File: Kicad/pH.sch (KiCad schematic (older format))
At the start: 3 parts, among them U1 MCP6241

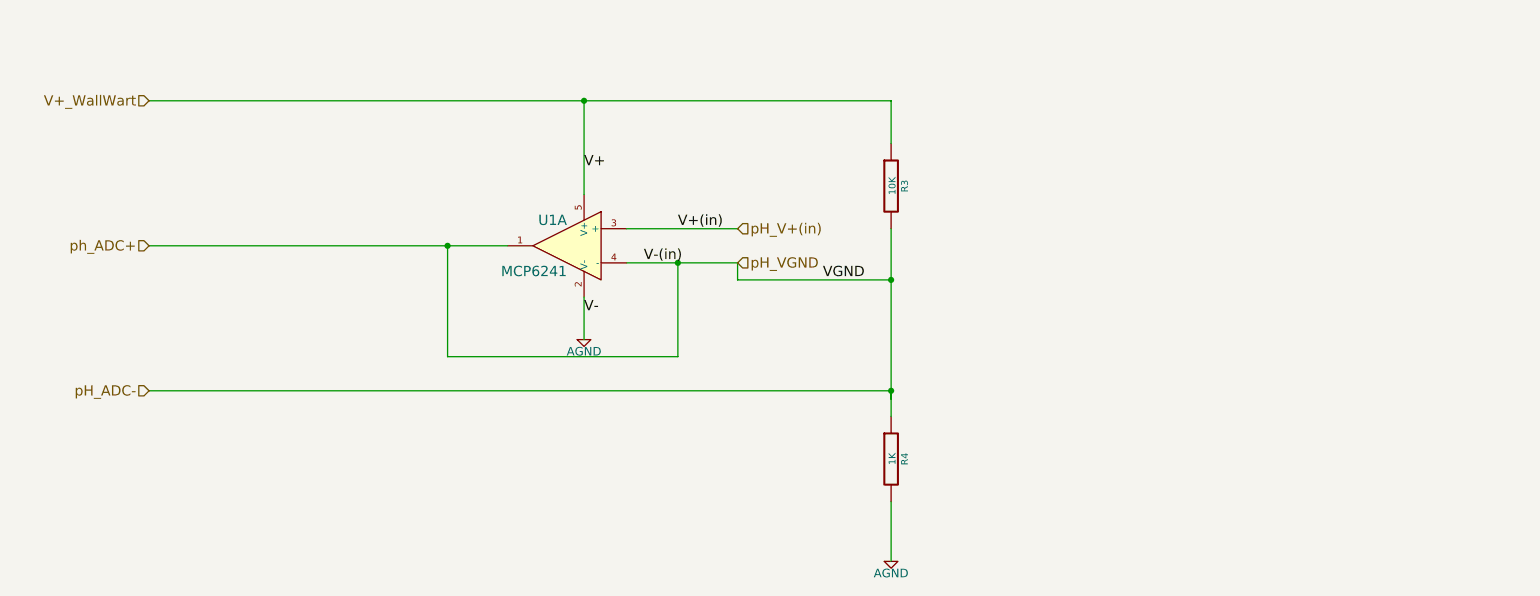
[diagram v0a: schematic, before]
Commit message: Layout with traces - ran through ERC and DRC
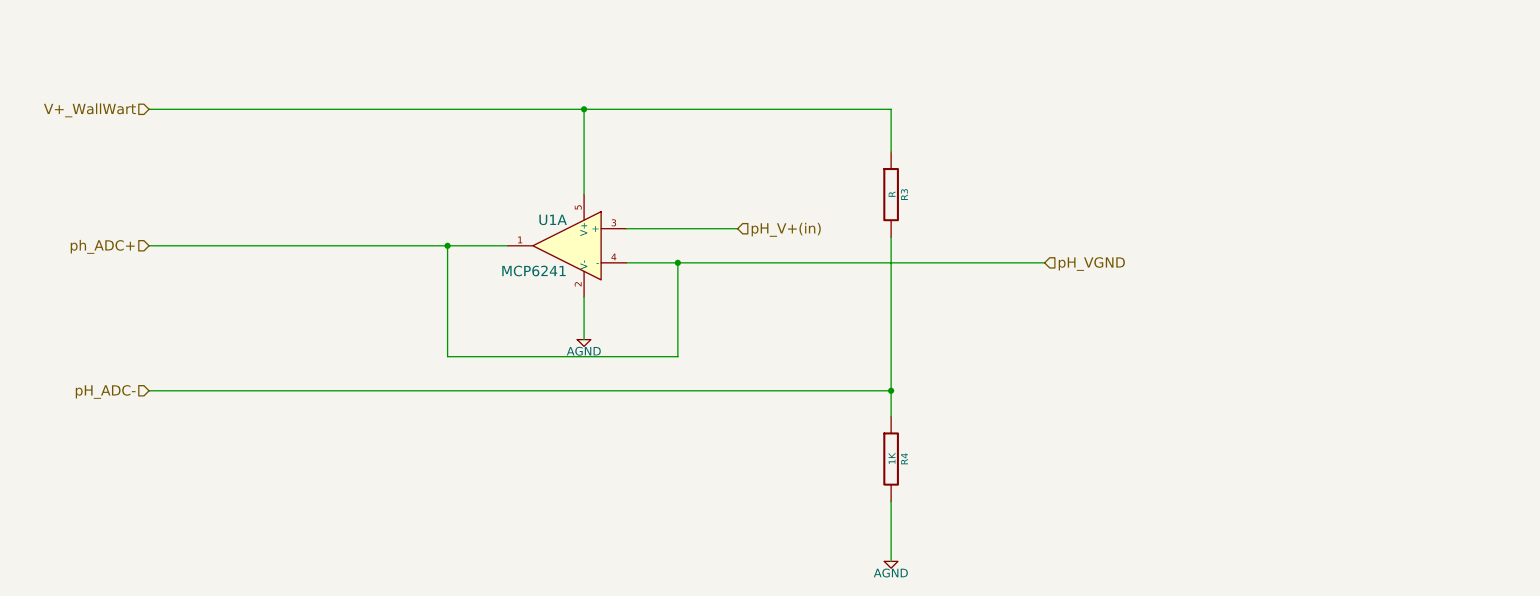
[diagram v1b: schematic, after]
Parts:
- R3: value 10K -> R
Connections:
- net labels removed: V+, V+(in), V-, V-(in), VGND
- wire segments 16 -> 13
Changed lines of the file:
@@
 Sheet 3 7
 Title ""
-Date "14 aug 2014"
+Date "19 aug 2014"
 Rev ""
 Comp ""
@@
 Comment4 ""
 $EndDescr
-Text HLabel 1350 2350 0    60   Input ~ 0
+Text HLabel 1350 2400 0    60   Input ~ 0
 V+_WallWart
 Text HLabel 1350 3200 0    60   Input ~ 0
@@
 	4450 3300 4450 3850
 Wire Wire Line
-	4150 3300 4800 3300
+	4150 3300 6600 3300
 Wire Wire Line
 	3900 3500 3900 3750
 Connection ~ 3100 3200
-Wire Wire Line
-	5700 2350 5700 2600
-$Comp
-L R R3
-U 1 1 53D7D144
-P 5700 2850
-F 0 "R3" V 5780 2850 40  0000 C CNN
-F 1 "10K" V 5707 2851 40  0000 C CNN
-F 2 "~" V 5630 2850 30  0000 C CNN
-F 3 "~" H 5700 2850 30  0000 C CNN
-	1    5700 2850
-	1    0    0    -1
-$EndComp
 $Comp
 L R R4
@@
 $EndComp
 Wire Wire Line
-	5700 3100 5700 4200
-Wire Wire Line
 	1350 3200 3450 3200
 Wire Wire Line
@@
 Text HLabel 1350 4050 0    60   Input ~ 0
 pH_ADC-
-Wire Wire Line
-	5700 4050 5700 4100
-Wire Wire Line
-	1350 4050 5700 4050
-Connection ~ 5700 4050
 $Comp
-L AGND #PWR8
+L AGND #PWR08
 U 1 1 53DCC7DA
 P 3900 3750
-F 0 "#PWR8" H 3900 3750 40  0001 C CNN
+F 0 "#PWR08" H 3900 3750 40  0001 C CNN
 F 1 "AGND" H 3900 3680 50  0000 C CNN
 F 2 "" H 3900 3750 60  0000 C CNN
@@
 $EndComp
 $Comp
-L AGND #PWR9
+L AGND #PWR09
 U 1 1 53DCC7F8
 P 5700 5050
-F 0 "#PWR9" H 5700 5050 40  0001 C CNN
+F 0 "#PWR09" H 5700 5050 40  0001 C CNN
 F 1 "AGND" H 5700 4980 50  0000 C CNN
 F 2 "" H 5700 5050 60  0000 C CNN
@@
 	1    0    0    -1
 $EndComp
-Wire Wire Line
-	1350 2350 5700 2350
-Wire Wire Line
-	3900 2350 3900 2900
-Connection ~ 3900 2350
-Text Label 5300 3400 0    60   ~ 0
-VGND
-Text Label 4450 3100 0    60   ~ 0
-V+(in)
-Text Label 3900 2750 0    60   ~ 0
-V+
-Text Label 3900 3600 0    60   ~ 0
-V-
-Text Label 4250 3300 0    60   ~ 0
-V-(in)
-Wire Wire Line
-	4800 3300 4800 3400
-Wire Wire Line
-	4800 3400 5700 3400
-Connection ~ 5700 3400
 Text HLabel 4800 3100 2    60   Input ~ 0
 pH_V+(in)
-Text HLabel 4800 3300 2    60   Input ~ 0
+Text HLabel 6600 3300 2    60   Input ~ 0
 pH_VGND
 Connection ~ 4450 3300
@@
 	-1   0    0    -1
 $EndComp
+$Comp
+L R R3
+U 1 1 53F37946
+P 5700 2900
+F 0 "R3" V 5780 2900 40  0000 C CNN
+F 1 "R" V 5707 2901 40  0000 C CNN
+F 2 "~" V 5630 2900 30  0000 C CNN
+F 3 "~" H 5700 2900 30  0000 C CNN
+	1    5700 2900
+	1    0    0    -1
+$EndComp
+Wire Wire Line
+	5700 3150 5700 4200
+Wire Wire Line
+	5700 2650 5700 2400
+Wire Wire Line
+	5700 2400 1350 2400
+Wire Wire Line
+	1350 4050 5700 4050
+Connection ~ 5700 4050
+Wire Wire Line
+	3900 2900 3900 2400
+Connection ~ 3900 2400
 $EndSCHEMATC

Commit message: Dev Rev 1
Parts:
- added TP1, TP8: CONN_1, symbol CONN_1
- R3: value R -> 10K
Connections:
- net pH_ADC-: now also TP8.1
- net pH_VGND: now also TP1.1
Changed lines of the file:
@@
 Sheet 3 7
 Title ""
-Date "20 aug 2014"
+Date "21 aug 2014"
 Rev ""
 Comp ""
@@
 P 5700 2900
 F 0 "R3" V 5780 2900 40  0000 C CNN
-F 1 "R" V 5707 2901 40  0000 C CNN
+F 1 "10K" V 5707 2901 40  0000 C CNN
 F 2 "~" V 5630 2900 30  0000 C CNN
 F 3 "~" H 5700 2900 30  0000 C CNN
@@
 	3900 2900 3900 2400
 Connection ~ 3900 2400
+$Comp
+L CONN_1 TP1
+U 1 1 53F5D6D1
+P 2350 2900
+F 0 "TP1" H 2430 2900 40  0000 L CNN
+F 1 "CONN_1" H 2350 2955 30  0001 C CNN
+F 2 "" H 2350 2900 60  0000 C CNN
+F 3 "" H 2350 2900 60  0000 C CNN
+	1    2350 2900
+	0    -1   -1   0
+$EndComp
+Wire Wire Line
+	2350 3050 2350 3200
+Connection ~ 2350 3200
+$Comp
+L CONN_1 TP8
+U 1 1 53F5D987
+P 2300 3750
+F 0 "TP8" H 2380 3750 40  0000 L CNN
+F 1 "CONN_1" H 2300 3805 30  0001 C CNN
+F 2 "" H 2300 3750 60  0000 C CNN
+F 3 "" H 2300 3750 60  0000 C CNN
+	1    2300 3750
+	0    -1   -1   0
+$EndComp
+Wire Wire Line
+	2300 3900 2300 4050
+Connection ~ 2300 4050
 $EndSCHEMATC

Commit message: updates for dev rev 2
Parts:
- removed TP8: CONN_1, symbol CONN_1
- added TP? (x2): CONN_1, symbol CONN_1
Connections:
- net pH_ADC- renamed pH_ADC_IN-
- net pH_V+(in) renamed pH_BNC_V
- net pH_BNC_V: now also TP?.1
- net pH_VGND renamed ph_ADC_IN+
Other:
- moved on the sheet: R3, R4
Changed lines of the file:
@@
 Sheet 3 7
 Title ""
-Date "21 aug 2014"
+Date "9 sep 2014"
 Rev ""
 Comp ""
@@
 Comment4 ""
 $EndDescr
-Text HLabel 1350 2400 0    60   Input ~ 0
+Text HLabel 3900 2400 0    60   Input ~ 0
 V+_WallWart
 Text HLabel 1350 3200 0    60   Input ~ 0
-ph_ADC+
-Wire Wire Line
-	3100 3200 3100 3850
-Wire Wire Line
-	4450 3300 4450 3850
-Wire Wire Line
-	4150 3300 6600 3300
+ph_ADC_IN+
 Wire Wire Line
 	3900 3500 3900 3750
-Connection ~ 3100 3200
 $Comp
 L R R4
 U 1 1 53D7D158
-P 5700 4450
-F 0 "R4" V 5780 4450 40  0000 C CNN
-F 1 "1K" V 5707 4451 40  0000 C CNN
-F 2 "~" V 5630 4450 30  0000 C CNN
-F 3 "~" H 5700 4450 30  0000 C CNN
-	1    5700 4450
+P 7450 3850
+F 0 "R4" V 7530 3850 40  0000 C CNN
+F 1 "1K" V 7457 3851 40  0000 C CNN
+F 2 "~" V 7380 3850 30  0000 C CNN
+F 3 "~" H 7450 3850 30  0000 C CNN
+	1    7450 3850
 	1    0    0    -1
 $EndComp
 Wire Wire Line
 	1350 3200 3450 3200
-Wire Wire Line
-	4150 3100 4800 3100
-Wire Wire Line
-	4450 3850 3100 3850
-Wire Wire Line
-	5700 4700 5700 5050
-Text HLabel 1350 4050 0    60   Input ~ 0
-pH_ADC-
+Text HLabel 7950 1900 0    60   Input ~ 0
+pH_ADC_IN-
 $Comp
 L AGND #PWR08
@@
 	1    0    0    -1
 $EndComp
-$Comp
-L AGND #PWR09
-U 1 1 53DCC7F8
-P 5700 5050
-F 0 "#PWR09" H 5700 5050 40  0001 C CNN
-F 1 "AGND" H 5700 4980 50  0000 C CNN
-F 2 "" H 5700 5050 60  0000 C CNN
-F 3 "" H 5700 5050 60  0000 C CNN
-	1    5700 5050
-	1    0    0    -1
-$EndComp
-Text HLabel 4800 3100 2    60   Input ~ 0
-pH_V+(in)
-Text HLabel 6600 3300 2    60   Input ~ 0
-pH_VGND
-Connection ~ 4450 3300
 $Comp
 L MCP6241 U1
@@
 L R R3
 U 1 1 53F37946
-P 5700 2900
-F 0 "R3" V 5780 2900 40  0000 C CNN
-F 1 "10K" V 5707 2901 40  0000 C CNN
-F 2 "~" V 5630 2900 30  0000 C CNN
-F 3 "~" H 5700 2900 30  0000 C CNN
-	1    5700 2900
+P 7450 2950
+F 0 "R3" V 7530 2950 40  0000 C CNN
+F 1 "10K" V 7457 2951 40  0000 C CNN
+F 2 "~" V 7380 2950 30  0000 C CNN
+F 3 "~" H 7450 2950 30  0000 C CNN
+	1    7450 2950
 	1    0    0    -1
 $EndComp
 Wire Wire Line
-	5700 3150 5700 4200
-Wire Wire Line
-	5700 2650 5700 2400
-Wire Wire Line
-	5700 2400 1350 2400
-Wire Wire Line
-	1350 4050 5700 4050
-Connection ~ 5700 4050
-Wire Wire Line
 	3900 2900 3900 2400
-Connection ~ 3900 2400
 $Comp
 L CONN_1 TP1
@@
 	2350 3050 2350 3200
 Connection ~ 2350 3200
+Wire Wire Line
+	7450 3200 7450 3600
+Text HLabel 7450 2450 0    60   Input ~ 0
+V+_WallWart
+Wire Wire Line
+	7450 2700 7450 2450
+Text HLabel 5700 3100 2    60   Input ~ 0
+pH_BNC_V
+Wire Wire Line
+	4150 3100 5700 3100
+Wire Wire Line
+	2950 3200 2950 4100
+Wire Wire Line
+	2950 4100 4750 4100
+Wire Wire Line
+	4750 4100 4750 3300
+Wire Wire Line
+	4750 3300 4150 3300
+Connection ~ 2950 3200
 $Comp
-L CONN_1 TP8
-U 1 1 53F5D987
-P 2300 3750
-F 0 "TP8" H 2380 3750 40  0000 L CNN
-F 1 "CONN_1" H 2300 3805 30  0001 C CNN
-F 2 "" H 2300 3750 60  0000 C CNN
-F 3 "" H 2300 3750 60  0000 C CNN
-	1    2300 3750
+L AGND #PWR?
+U 1 1 540C92AB
+P 7450 4400
+F 0 "#PWR?" H 7450 4400 40  0001 C CNN
+F 1 "AGND" H 7450 4330 50  0000 C CNN
+F 2 "" H 7450 4400 60  0000 C CNN
+F 3 "" H 7450 4400 60  0000 C CNN
+	1    7450 4400
+	1    0    0    -1
+$EndComp
+Wire Wire Line
+	7450 4400 7450 4100
+Text HLabel 8600 3400 2    60   Input ~ 0
+pH_BNC_GND
+$Comp
+L CONN_1 TP?
+U 1 1 540C941C
+P 8200 2900
+F 0 "TP?" H 8280 2900 40  0000 L CNN
+F 1 "CONN_1" H 8200 2955 30  0001 C CNN
+F 2 "" H 8200 2900 60  0000 C CNN
+F 3 "" H 8200 2900 60  0000 C CNN
+	1    8200 2900
+	1    0    0    -1
+$EndComp
+Wire Wire Line
+	8050 1900 8050 3400
+$Comp
+L CONN_1 TP?
+U 1 1 540C9446
+P 5150 2750
+F 0 "TP?" H 5230 2750 40  0000 L CNN
+F 1 "CONN_1" H 5150 2805 30  0001 C CNN
+F 2 "" H 5150 2750 60  0000 C CNN
+F 3 "" H 5150 2750 60  0000 C CNN
+	1    5150 2750
 	0    -1   -1   0
 $EndComp
 Wire Wire Line
-	2300 3900 2300 4050
-Connection ~ 2300 4050
+	5150 2900 5150 3100
+Connection ~ 5150 3100
+Wire Wire Line
+	8050 1900 7950 1900
+Text Label 7650 3350 0    60   ~ 0
+.45V
+Wire Wire Line
+	7450 3400 8600 3400
+Connection ~ 7450 3400
+Connection ~ 8050 3400
 $EndSCHEMATC

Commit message: Ready for Schematic Design Review
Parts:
- gave numbers to parts that had none: 2
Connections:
- net pH_ADC_IN-: now also TP18.1
- net pH_BNC_V renamed pH_Probe_V
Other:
- moved on the sheet: TP18
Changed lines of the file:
@@
 $Descr A4 11693 8268
 encoding utf-8
-Sheet 3 7
+Sheet 7 7
 Title ""
-Date "9 sep 2014"
+Date "10 sep 2014"
 Rev ""
 Comp ""
@@
 pH_ADC_IN-
 $Comp
-L AGND #PWR08
+L AGND #PWR07
 U 1 1 53DCC7DA
 P 3900 3750
-F 0 "#PWR08" H 3900 3750 40  0001 C CNN
+F 0 "#PWR07" H 3900 3750 40  0001 C CNN
 F 1 "AGND" H 3900 3680 50  0000 C CNN
 F 2 "" H 3900 3750 60  0000 C CNN
@@
 	7450 2700 7450 2450
 Text HLabel 5700 3100 2    60   Input ~ 0
-pH_BNC_V
+pH_Probe_V
 Wire Wire Line
 	4150 3100 5700 3100
@@
 Connection ~ 2950 3200
 $Comp
-L AGND #PWR?
+L AGND #PWR08
 U 1 1 540C92AB
 P 7450 4400
-F 0 "#PWR?" H 7450 4400 40  0001 C CNN
+F 0 "#PWR08" H 7450 4400 40  0001 C CNN
 F 1 "AGND" H 7450 4330 50  0000 C CNN
 F 2 "" H 7450 4400 60  0000 C CNN
@@
 	7450 4400 7450 4100
 Text HLabel 8600 3400 2    60   Input ~ 0
-pH_BNC_GND
+pH_Probe_GND
 $Comp
-L CONN_1 TP?
+L CONN_1 TP18
 U 1 1 540C941C
-P 8200 2900
-F 0 "TP?" H 8280 2900 40  0000 L CNN
-F 1 "CONN_1" H 8200 2955 30  0001 C CNN
-F 2 "" H 8200 2900 60  0000 C CNN
-F 3 "" H 8200 2900 60  0000 C CNN
-	1    8200 2900
+P 8500 2900
+F 0 "TP18" H 8580 2900 40  0000 L CNN
+F 1 "CONN_1" H 8500 2955 30  0001 C CNN
+F 2 "" H 8500 2900 60  0000 C CNN
+F 3 "" H 8500 2900 60  0000 C CNN
+	1    8500 2900
 	1    0    0    -1
 $EndComp
@@
 	8050 1900 8050 3400
 $Comp
-L CONN_1 TP?
+L CONN_1 TP17
 U 1 1 540C9446
 P 5150 2750
-F 0 "TP?" H 5230 2750 40  0000 L CNN
+F 0 "TP17" H 5230 2750 40  0000 L CNN
 F 1 "CONN_1" H 5150 2805 30  0001 C CNN
 F 2 "" H 5150 2750 60  0000 C CNN
@@
 Wire Wire Line
 	8050 1900 7950 1900
-Text Label 7650 3350 0    60   ~ 0
-.45V
 Wire Wire Line
 	7450 3400 8600 3400
 Connection ~ 7450 3400
 Connection ~ 8050 3400
+Wire Wire Line
+	8350 2900 8350 3400
+Connection ~ 8350 3400
 $EndSCHEMATC
